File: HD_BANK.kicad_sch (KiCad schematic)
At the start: 1 part, among them J8 DF40HC(3.0)-120DS

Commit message: finishing schematic
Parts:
- removed J8: DF40HC(3.0)-120DS, Connector_Hirose_DF40:Hirose_DF40C-120DS-0.4V_2x60_P0.4mm, symbol dfdtc_Connector:Conn_02x60_Odd_Even
- added J6: FX8-140P-SV1, Connector_Hirose_FX8:Hirose_FX8-140P-SV_2x70_P0.6mm, symbol dfdtc_Connector:Conn_02x70_Odd_Even
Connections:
- new net +5V: J6.105 (Pin_105), J6.106 (Pin_106), J6.107 (Pin_107), J6.108 (Pin_108), J6.109 (Pin_109), J6.110 (Pin_110), J6.111 (Pin_111), J6.112 (Pin_112), J6.113 (Pin_113), J6.114 (Pin_114), J6.115 (Pin_115), J6.116 (Pin_116), J6.117 (Pin_117), J6.118 (Pin_118), J6.119 (Pin_119), J6.120 (Pin_120), J6.121, J6.122, J6.123, J6.124, J6.125, J6.126, J6.127, J6.128, J6.129, J6.130, J6.131, J6.132, J6.133, J6.134, J6.135, J6.136, J6.137, J6.138, J6.139, J6.140
- new net FAN_PWM: J6.87 (Pin_87)
- new net FAN_TACH: J6.89 (Pin_89)
- new net GND: J6.1 (Pin_1), J6.100 (Pin_100), J6.101 (Pin_101), J6.102 (Pin_102), J6.103 (Pin_103), J6.104 (Pin_104), J6.11 (Pin_11), J6.12 (Pin_12), J6.2 (Pin_2), J6.21 (Pin_21), J6.22 (Pin_22), J6.31 (Pin_31), J6.32 (Pin_32), J6.41 (Pin_41), J6.42 (Pin_42), J6.51 (Pin_51), J6.52 (Pin_52), J6.61 (Pin_61), J6.62 (Pin_62), J6.71 (Pin_71), J6.72 (Pin_72), J6.77 (Pin_77), J6.78 (Pin_78), J6.81 (Pin_81), J6.82 (Pin_82), J6.91 (Pin_91), J6.92 (Pin_92), J6.97 (Pin_97), J6.98 (Pin_98), J6.99 (Pin_99)
- new net IO_L10N_AD10N_87_N: J6.65 (Pin_65)
- new net IO_L10N_AD2N_84_N: J6.49 (Pin_49)
- new net IO_L10N_AD2N_86_N: J6.50 (Pin_50)
- new net IO_L10P_AD10P_87_P: J6.63 (Pin_63)
- new net IO_L10P_AD2P_84_P: J6.47 (Pin_47)
- new net IO_L10P_AD2P_86_P: J6.48 (Pin_48)
- new net IO_L11N_AD1N_84_N: J6.55 (Pin_55)
- new net IO_L11N_AD1N_86_N: J6.56 (Pin_56)
- new net IO_L11N_AD9N_87_N: J6.69 (Pin_69)
- new net IO_L11P_AD1P_84_P: J6.53 (Pin_53)
- new net IO_L11P_AD1P_86_P: J6.54 (Pin_54)
- new net IO_L11P_AD9P_87_P: J6.67 (Pin_67)
- new net IO_L12N_AD0N_84_N: J6.59 (Pin_59)
- new net IO_L12N_AD0N_86_N: J6.60 (Pin_60)
- new net IO_L12N_AD8N_87_N: J6.75 (Pin_75)
- new net IO_L12P_AD0P_84_P: J6.57 (Pin_57)
- new net IO_L12P_AD0P_86_P: J6.58 (Pin_58)
- new net IO_L12P_AD8P_87_P: J6.73 (Pin_73)
- new net IO_L1N_AD11N_84_N: J6.5 (Pin_5)
- new net IO_L1N_AD11N_86_N: J6.6 (Pin_6)
- new net IO_L1P_AD11P_84_P: J6.3 (Pin_3)
- new net IO_L1P_AD11P_86_P: J6.4 (Pin_4)
- new net IO_L2N_AD10N_84_N: J6.9 (Pin_9)
- new net IO_L2N_AD10N_86_N: J6.10 (Pin_10)
- new net IO_L2P_AD10P_84_P: J6.7 (Pin_7)
- new net IO_L2P_AD10P_86_P: J6.8 (Pin_8)
- new net IO_L3N_AD9N_84_N: J6.15 (Pin_15)
- new net IO_L3N_AD9N_86_N: J6.16 (Pin_16)
- new net IO_L3P_AD9P_84_P: J6.13 (Pin_13)
- new net IO_L3P_AD9P_86_P: J6.14 (Pin_14)
- new net IO_L4N_AD8N_84_N: J6.19 (Pin_19)
- new net IO_L4N_AD8N_86_N: J6.20 (Pin_20)
- new net IO_L4P_AD8P_84_P: J6.17 (Pin_17)
- new net IO_L4P_AD8P_86_P: J6.18 (Pin_18)
- new net IO_L5N_HDGC_AD7N_84_N: J6.25 (Pin_25)
- new net IO_L5N_HDGC_AD7N_86_N: J6.26 (Pin_26)
- new net IO_L5P_HDGC_AD7P_84_P: J6.23 (Pin_23)
- new net IO_L5P_HDGC_AD7P_86_P: J6.24 (Pin_24)
- new net IO_L6N_HDGC_87_N: J6.86 (Pin_86)
- new net IO_L6N_HDGC_AD6N_84_N: J6.29 (Pin_29)
- new net IO_L6N_HDGC_AD6N_86_N: J6.30 (Pin_30)
- new net IO_L6P_HDGC_AD6P_84_P: J6.27 (Pin_27)
- new net IO_L6P_HDGC_AD6P_86_P: J6.28 (Pin_28)
- new net IO_L7N_HDGC_87_N: J6.66 (Pin_66)
- new net IO_L7N_HDGC_AD5N_84_N: J6.35 (Pin_35)
- new net IO_L7N_HDGC_AD5N_86_N: J6.36 (Pin_36)
- new net IO_L7P_HDGC_87_P: J6.64 (Pin_64)
- new net IO_L7P_HDGC_AD5P_84_P: J6.33 (Pin_33)
- new net IO_L7P_HDGC_AD5P_86_P: J6.34 (Pin_34)
- new net IO_L8N_HDGC_87_N: J6.70 (Pin_70)
- new net IO_L8N_HDGC_AD4N_84_N: J6.39 (Pin_39)
- new net IO_L8N_HDGC_AD4N_86_N: J6.40 (Pin_40)
- new net IO_L8P_HDGC_87_P: J6.68 (Pin_68)
- new net IO_L8P_HDGC_AD4P_84_P: J6.37 (Pin_37)
- new net IO_L8P_HDGC_AD4P_86_P: J6.38 (Pin_38)
- new net IO_L9N_AD11N_87_N: J6.76 (Pin_76)
- new net IO_L9N_AD3N_84_N: J6.45 (Pin_45)
- new net IO_L9N_AD3N_86_N: J6.46 (Pin_46)
- new net IO_L9P_AD11P_87_P: J6.74 (Pin_74)
- new net IO_L9P_AD3P_84_P: J6.43 (Pin_43)
- new net IO_L9P_AD3P_86_P: J6.44 (Pin_44)
- new net P1_GPIO: J6.85 (Pin_85)
- new net P1_INT: J6.83 (Pin_83)
- new net PMIC_32KOUT: J6.84 (Pin_84)
- new net PMIC_PWRKY: J6.94 (Pin_94)
- new net Power_SCL: J6.90 (Pin_90)
- new net Power_SDA: J6.88 (Pin_88)
- new net VBAT: J6.96 (Pin_96)
- new net VCCO_HD: J6.79 (Pin_79), J6.80 (Pin_80)

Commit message: sync works
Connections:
- net GND: now also J6.105 (Pin_105), J6.106 (Pin_106), J6.107 (Pin_107), J6.108 (Pin_108), J6.109 (Pin_109), J6.110 (Pin_110), J6.111 (Pin_111), J6.112 (Pin_112), J6.113 (Pin_113), J6.114 (Pin_114), J6.115 (Pin_115), J6.116 (Pin_116), J6.117 (Pin_117), J6.118 (Pin_118), J6.119 (Pin_119), J6.120 (Pin_120), J6.121, J6.122
- net PROGRAM_B_0: now reaches J6.93 (Pin_93)
- net SYS_PG: now reaches J6.95 (Pin_95)
- net +5V renamed +12V
- net +12V: no longer J6.105 (Pin_105), J6.106 (Pin_106), J6.107 (Pin_107), J6.108 (Pin_108), J6.109 (Pin_109), J6.110 (Pin_110), J6.111 (Pin_111), J6.112 (Pin_112), J6.113 (Pin_113), J6.114 (Pin_114), J6.115 (Pin_115), J6.116 (Pin_116), J6.117 (Pin_117), J6.118 (Pin_118), J6.119 (Pin_119), J6.120 (Pin_120), J6.121, J6.122

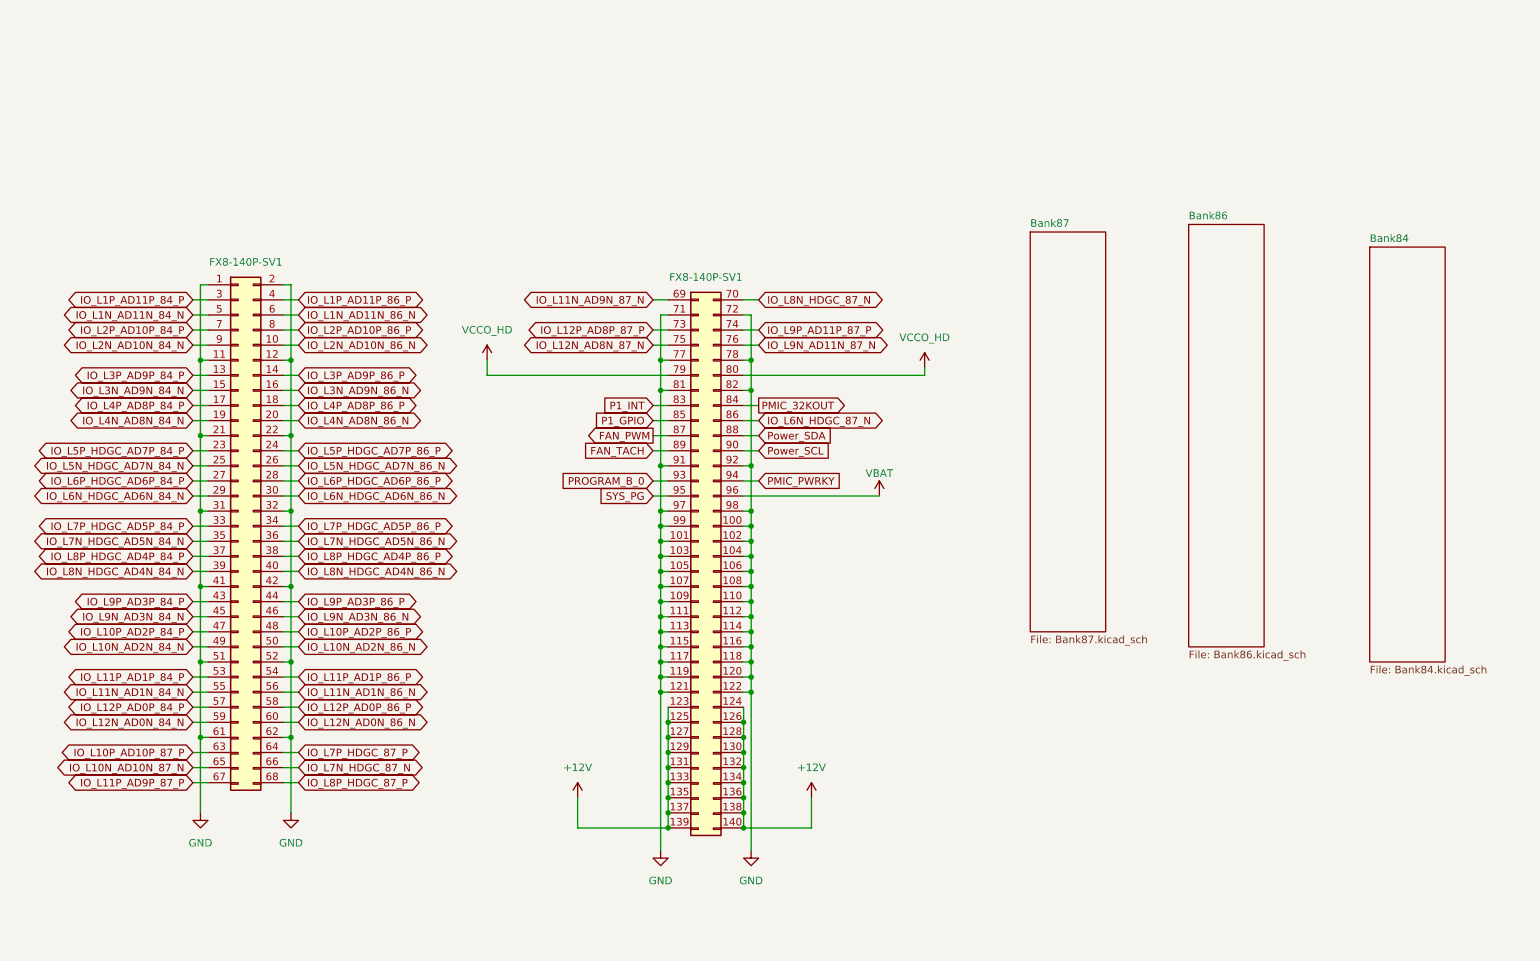
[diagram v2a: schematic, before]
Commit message: change net name to of IO diff pairs, add a scripts for name modification
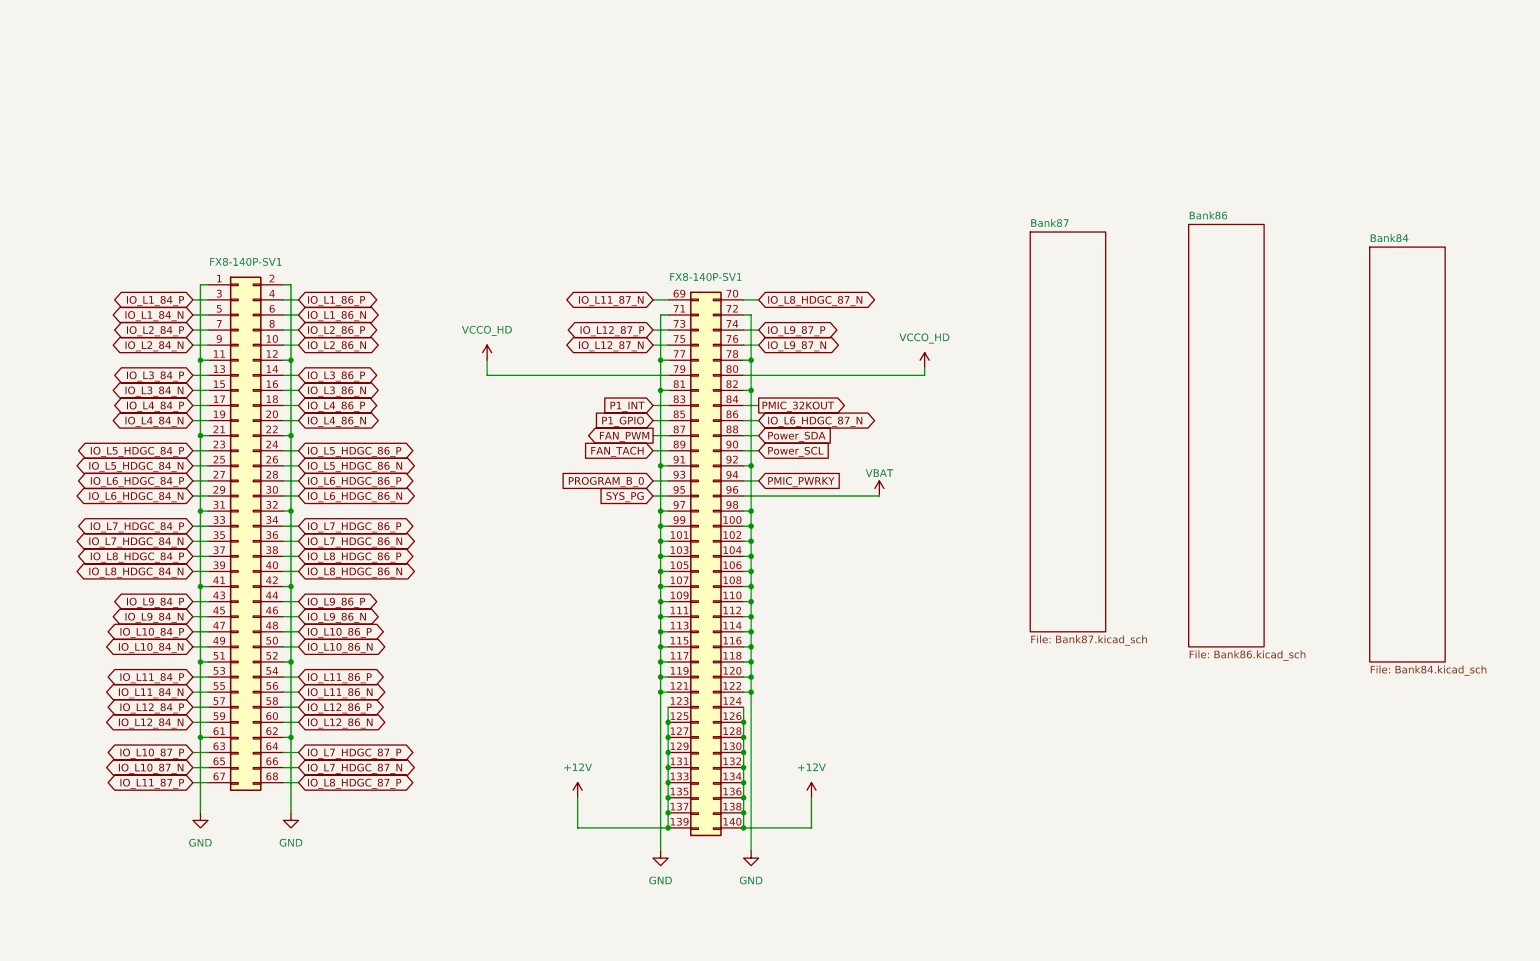
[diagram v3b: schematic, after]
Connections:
- net IO_L10N_AD10N_87_N renamed IO_L10_87_N
- net IO_L10N_AD2N_84_N renamed IO_L10_84_N
- net IO_L10N_AD2N_86_N renamed IO_L10_86_N
- net IO_L10P_AD10P_87_P renamed IO_L10_87_P
- net IO_L10P_AD2P_84_P renamed IO_L10_84_P
- net IO_L10P_AD2P_86_P renamed IO_L10_86_P
- net IO_L11N_AD1N_84_N renamed IO_L11_84_N
- net IO_L11N_AD1N_86_N renamed IO_L11_86_N
- net IO_L11N_AD9N_87_N renamed IO_L11_87_N
- net IO_L11P_AD1P_84_P renamed IO_L11_84_P
- net IO_L11P_AD1P_86_P renamed IO_L11_86_P
- net IO_L11P_AD9P_87_P renamed IO_L11_87_P
- net IO_L12N_AD0N_84_N renamed IO_L12_84_N
- net IO_L12N_AD0N_86_N renamed IO_L12_86_N
- net IO_L12N_AD8N_87_N renamed IO_L12_87_N
- net IO_L12P_AD0P_84_P renamed IO_L12_84_P
- net IO_L12P_AD0P_86_P renamed IO_L12_86_P
- net IO_L12P_AD8P_87_P renamed IO_L12_87_P
- net IO_L1N_AD11N_84_N renamed IO_L1_84_N
- net IO_L1N_AD11N_86_N renamed IO_L1_86_N
- net IO_L1P_AD11P_84_P renamed IO_L1_84_P
- net IO_L1P_AD11P_86_P renamed IO_L1_86_P
- net IO_L2N_AD10N_84_N renamed IO_L2_84_N
- net IO_L2N_AD10N_86_N renamed IO_L2_86_N
- net IO_L2P_AD10P_84_P renamed IO_L2_84_P
- net IO_L2P_AD10P_86_P renamed IO_L2_86_P
- net IO_L3N_AD9N_84_N renamed IO_L3_84_N
- net IO_L3N_AD9N_86_N renamed IO_L3_86_N
- net IO_L3P_AD9P_84_P renamed IO_L3_84_P
- net IO_L3P_AD9P_86_P renamed IO_L3_86_P
- net IO_L4N_AD8N_84_N renamed IO_L4_84_N
- net IO_L4N_AD8N_86_N renamed IO_L4_86_N
- net IO_L4P_AD8P_84_P renamed IO_L4_84_P
- net IO_L4P_AD8P_86_P renamed IO_L4_86_P
- net IO_L5N_HDGC_AD7N_84_N renamed IO_L5_HDGC_84_N
- net IO_L5N_HDGC_AD7N_86_N renamed IO_L5_HDGC_86_N
- net IO_L5P_HDGC_AD7P_84_P renamed IO_L5_HDGC_84_P
- net IO_L5P_HDGC_AD7P_86_P renamed IO_L5_HDGC_86_P
- net IO_L6N_HDGC_87_N renamed IO_L6_HDGC_87_N
- net IO_L6N_HDGC_AD6N_84_N renamed IO_L6_HDGC_84_N
- net IO_L6N_HDGC_AD6N_86_N renamed IO_L6_HDGC_86_N
- net IO_L6P_HDGC_AD6P_84_P renamed IO_L6_HDGC_84_P
- net IO_L6P_HDGC_AD6P_86_P renamed IO_L6_HDGC_86_P
- net IO_L7N_HDGC_87_N renamed IO_L7_HDGC_87_N
- net IO_L7N_HDGC_AD5N_84_N renamed IO_L7_HDGC_84_N
- net IO_L7N_HDGC_AD5N_86_N renamed IO_L7_HDGC_86_N
- net IO_L7P_HDGC_87_P renamed IO_L7_HDGC_87_P
- net IO_L7P_HDGC_AD5P_84_P renamed IO_L7_HDGC_84_P
- net IO_L7P_HDGC_AD5P_86_P renamed IO_L7_HDGC_86_P
- net IO_L8N_HDGC_87_N renamed IO_L8_HDGC_87_N
- net IO_L8N_HDGC_AD4N_84_N renamed IO_L8_HDGC_84_N
- net IO_L8N_HDGC_AD4N_86_N renamed IO_L8_HDGC_86_N
- net IO_L8P_HDGC_87_P renamed IO_L8_HDGC_87_P
- net IO_L8P_HDGC_AD4P_84_P renamed IO_L8_HDGC_84_P
- net IO_L8P_HDGC_AD4P_86_P renamed IO_L8_HDGC_86_P
- net IO_L9N_AD11N_87_N renamed IO_L9_87_N
- net IO_L9N_AD3N_84_N renamed IO_L9_84_N
- net IO_L9N_AD3N_86_N renamed IO_L9_86_N
- net IO_L9P_AD11P_87_P renamed IO_L9_87_P
- net IO_L9P_AD3P_84_P renamed IO_L9_84_P
- net IO_L9P_AD3P_86_P renamed IO_L9_86_P
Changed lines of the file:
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@@
 		)
 	)
-	(global_label "IO_L3P_AD9P_84_P"
+	(global_label "IO_L3_84_P"
 		(shape bidirectional)
 		(at 55.88 95.25 180)
@@
 		)
 	)
-	(global_label "IO_L4P_AD8P_84_P"
+	(global_label "IO_L4_84_P"
 		(shape bidirectional)
 		(at 55.88 100.33 180)
@@
 		)
 	)
-	(global_label "IO_L1N_AD11N_86_N"
+	(global_label "IO_L1_86_N"
 		(shape bidirectional)
 		(at 73.66 85.09 0)
@@
 		)
 	)
-	(global_label "IO_L7N_HDGC_87_N"
+	(global_label "IO_L7_HDGC_87_N"
 		(shape bidirectional)
 		(at 73.66 161.29 0)
@@
 		)
 	)
-	(global_label "IO_L9N_AD11N_87_N"
+	(global_label "IO_L9_87_N"
 		(shape bidirectional)
 		(at 151.13 90.17 0)
@@
 		)
 	)
-	(global_label "IO_L9P_AD11P_87_P"
+	(global_label "IO_L9_87_P"
 		(shape bidirectional)
 		(at 151.13 87.63 0)
@@
 		)
 	)
-	(global_label "IO_L5N_HDGC_AD7N_86_N"
+	(global_label "IO_L5_HDGC_86_N"
 		(shape bidirectional)
 		(at 73.66 110.49 0)
@@
 		)
 	)
-	(global_label "IO_L6P_HDGC_AD6P_86_P"
+	(global_label "IO_L6_HDGC_86_P"
 		(shape bidirectional)
 		(at 73.66 113.03 0)
@@
 		)
 	)
-	(global_label "IO_L6N_HDGC_87_N"
+	(global_label "IO_L6_HDGC_87_N"
 		(shape bidirectional)
 		(at 151.13 102.87 0)
@@
 		)
 	)
-	(global_label "IO_L12N_AD8N_87_N"
+	(global_label "IO_L12_87_N"
 		(shape bidirectional)
 		(at 133.35 90.17 180)
@@
 		)
 	)
-	(global_label "IO_L11P_AD1P_84_P"
+	(global_label "IO_L11_84_P"
 		(shape bidirectional)
 		(at 55.88 146.05 180)
@@
 		)
 	)
-	(global_label "IO_L8P_HDGC_AD4P_86_P"
+	(global_label "IO_L8_HDGC_86_P"
 		(shape bidirectional)
 		(at 73.66 125.73 0)
@@
 		)
 	)
-	(global_label "IO_L4N_AD8N_86_N"
+	(global_label "IO_L4_86_N"
 		(shape bidirectional)
 		(at 73.66 102.87 0)
@@
 		)
 	)
-	(global_label "IO_L9P_AD3P_86_P"
+	(global_label "IO_L9_86_P"
 		(shape bidirectional)
 		(at 73.66 133.35 0)
@@
 		)
 	)
-	(global_label "IO_L7P_HDGC_AD5P_86_P"
+	(global_label "IO_L7_HDGC_86_P"
 		(shape bidirectional)
 		(at 73.66 120.65 0)
@@
 		)
 	)
-	(global_label "IO_L2P_AD10P_84_P"
+	(global_label "IO_L2_84_P"
 		(shape bidirectional)
 		(at 55.88 87.63 180)
@@
 		)
 	)
-	(global_label "IO_L8N_HDGC_AD4N_84_N"
+	(global_label "IO_L8_HDGC_84_N"
 		(shape bidirectional)
 		(at 55.88 128.27 180)
@@
 		)
 	)
-	(global_label "IO_L10N_AD2N_86_N"
+	(global_label "IO_L10_86_N"
 		(shape bidirectional)
 		(at 73.66 140.97 0)
@@
 		)
 	)
-	(global_label "IO_L12N_AD0N_84_N"
+	(global_label "IO_L12_84_N"
 		(shape bidirectional)
 		(at 55.88 153.67 180)
@@
 		)
 	)
-	(global_label "IO_L11N_AD1N_84_N"
+	(global_label "IO_L11_84_N"
 		(shape bidirectional)
 		(at 55.88 148.59 180)
@@
 		)
 	)
-	(global_label "IO_L7N_HDGC_AD5N_86_N"
+	(global_label "IO_L7_HDGC_86_N"
 		(shape bidirectional)
 		(at 73.66 123.19 0)
@@
 		)
 	)
-	(global_label "IO_L7N_HDGC_AD5N_84_N"
+	(global_label "IO_L7_HDGC_84_N"
 		(shape bidirectional)
 		(at 55.88 123.19 180)
@@
 		)
 	)
-	(global_label "IO_L12P_AD0P_84_P"
+	(global_label "IO_L12_84_P"
 		(shape bidirectional)
 		(at 55.88 151.13 180)
@@
 		)
 	)
-	(global_label "IO_L11P_AD1P_86_P"
+	(global_label "IO_L11_86_P"
 		(shape bidirectional)
 		(at 73.66 146.05 0)
@@
 		)
 	)
-	(global_label "IO_L10P_AD10P_87_P"
+	(global_label "IO_L10_87_P"
 		(shape bidirectional)
 		(at 55.88 158.75 180)
@@
 		)
 	)
-	(global_label "IO_L11N_AD9N_87_N"
+	(global_label "IO_L11_87_N"
 		(shape bidirectional)
 		(at 133.35 82.55 180)
@@
 		)
 	)
-	(global_label "IO_L1P_AD11P_84_P"
+	(global_label "IO_L1_84_P"
 		(shape bidirectional)
 		(at 55.88 82.55 180)
@@
 		)
 	)
-	(global_label "IO_L4N_AD8N_84_N"
+	(global_label "IO_L4_84_N"
 		(shape bidirectional)
 		(at 55.88 102.87 180)
@@
 		)
 	)
-	(global_label "IO_L4P_AD8P_86_P"
+	(global_label "IO_L4_86_P"
 		(shape bidirectional)
 		(at 73.66 100.33 0)
@@
 		)
 	)
-	(global_label "IO_L3P_AD9P_86_P"
+	(global_label "IO_L3_86_P"
 		(shape bidirectional)
 		(at 73.66 95.25 0)
@@
 		)
 	)
-	(global_label "IO_L10N_AD10N_87_N"
+	(global_label "IO_L10_87_N"
 		(shape bidirectional)
 		(at 55.88 161.29 180)
@@
 		)
 	)
-	(global_label "IO_L11P_AD9P_87_P"
+	(global_label "IO_L11_87_P"
 		(shape bidirectional)
 		(at 55.88 163.83 180)
@@
 		)
 	)
-	(global_label "IO_L2N_AD10N_86_N"
+	(global_label "IO_L2_86_N"
 		(shape bidirectional)
 		(at 73.66 90.17 0)
@@
 		)
 	)
-	(global_label "IO_L2P_AD10P_86_P"
+	(global_label "IO_L2_86_P"
 		(shape bidirectional)
 		(at 73.66 87.63 0)
@@
 		)
 	)
-	(global_label "IO_L3N_AD9N_86_N"
+	(global_label "IO_L3_86_N"
 		(shape bidirectional)
 		(at 73.66 97.79 0)
@@
 		)
 	)
-	(global_label "IO_L12N_AD0N_86_N"
+	(global_label "IO_L12_86_N"
 		(shape bidirectional)
 		(at 73.66 153.67 0)
@@
 		)
 	)
-	(global_label "IO_L8P_HDGC_AD4P_84_P"
+	(global_label "IO_L8_HDGC_84_P"
 		(shape bidirectional)
 		(at 55.88 125.73 180)
@@
 		)
 	)
-	(global_label "IO_L9P_AD3P_84_P"
+	(global_label "IO_L9_84_P"
 		(shape bidirectional)
 		(at 55.88 133.35 180)
@@
 		)
 	)
-	(global_label "IO_L7P_HDGC_87_P"
+	(global_label "IO_L7_HDGC_87_P"
 		(shape bidirectional)
 		(at 73.66 158.75 0)
@@
 		)
 	)
-	(global_label "IO_L5P_HDGC_AD7P_84_P"
+	(global_label "IO_L5_HDGC_84_P"
 		(shape bidirectional)
 		(at 55.88 107.95 180)
@@
 		)
 	)
-	(global_label "IO_L8N_HDGC_87_N"
+	(global_label "IO_L8_HDGC_87_N"
 		(shape bidirectional)
 		(at 151.13 82.55 0)
@@
 		)
 	)
-	(global_label "IO_L3N_AD9N_84_N"
+	(global_label "IO_L3_84_N"
 		(shape bidirectional)
 		(at 55.88 97.79 180)
@@
 		)
 	)
-	(global_label "IO_L9N_AD3N_86_N"
+	(global_label "IO_L9_86_N"
 		(shape bidirectional)
 		(at 73.66 135.89 0)
@@
 		)
 	)
-	(global_label "IO_L11N_AD1N_86_N"
+	(global_label "IO_L11_86_N"
 		(shape bidirectional)
 		(at 73.66 148.59 0)
@@
 		)
 	)
-	(global_label "IO_L7P_HDGC_AD5P_84_P"
+	(global_label "IO_L7_HDGC_84_P"
 		(shape bidirectional)
 		(at 55.88 120.65 180)
@@
 		)
 	)
-	(global_label "IO_L12P_AD8P_87_P"
+	(global_label "IO_L12_87_P"
 		(shape bidirectional)
 		(at 133.35 87.63 180)
@@
 		)
 	)
-	(global_label "IO_L6P_HDGC_AD6P_84_P"
+	(global_label "IO_L6_HDGC_84_P"
 		(shape bidirectional)
 		(at 55.88 113.03 180)
@@
 		)
 	)
-	(global_label "IO_L10P_AD2P_86_P"
+	(global_label "IO_L10_86_P"
 		(shape bidirectional)
 		(at 73.66 138.43 0)
@@
 		)
 	)
-	(global_label "IO_L9N_AD3N_84_N"
+	(global_label "IO_L9_84_N"
 		(shape bidirectional)
 		(at 55.88 135.89 180)
@@
 		)
 	)
-	(global_label "IO_L1P_AD11P_86_P"
+	(global_label "IO_L1_86_P"
 		(shape bidirectional)
 		(at 73.66 82.55 0)
@@
 		)
 	)
-	(global_label "IO_L5N_HDGC_AD7N_84_N"
+	(global_label "IO_L5_HDGC_84_N"
 		(shape bidirectional)
 		(at 55.88 110.49 180)
@@
 		)
 	)
-	(global_label "IO_L5P_HDGC_AD7P_86_P"
+	(global_label "IO_L5_HDGC_86_P"
 		(shape bidirectional)
 		(at 73.66 107.95 0)
@@
 		)
 	)
-	(global_label "IO_L10P_AD2P_84_P"
+	(global_label "IO_L10_84_P"
 		(shape bidirectional)
 		(at 55.88 138.43 180)
@@
 		)
 	)
-	(global_label "IO_L6N_HDGC_AD6N_84_N"
+	(global_label "IO_L6_HDGC_84_N"
 		(shape bidirectional)
 		(at 55.88 115.57 180)
@@
 		)
 	)
-	(global_label "IO_L8P_HDGC_87_P"
+	(global_label "IO_L8_HDGC_87_P"
 		(shape bidirectional)
 		(at 73.66 163.83 0)
@@
 		)
 	)
-	(global_label "IO_L6N_HDGC_AD6N_86_N"
+	(global_label "IO_L6_HDGC_86_N"
 		(shape bidirectional)
 		(at 73.66 115.57 0)
@@
 		)
 	)
-	(global_label "IO_L10N_AD2N_84_N"
+	(global_label "IO_L10_84_N"
 		(shape bidirectional)
 		(at 55.88 140.97 180)
@@
 		)
 	)
-	(global_label "IO_L2N_AD10N_84_N"
+	(global_label "IO_L2_84_N"
 		(shape bidirectional)
 		(at 55.88 90.17 180)
@@
 		)
 	)
-	(global_label "IO_L1N_AD11N_84_N"
+	(global_label "IO_L1_84_N"
 		(shape bidirectional)
 		(at 55.88 85.09 180)
@@
 		)
 	)
-	(global_label "IO_L8N_HDGC_AD4N_86_N"
+	(global_label "IO_L8_HDGC_86_N"
 		(shape bidirectional)
 		(at 73.66 128.27 0)
@@
 		)
 	)
-	(global_label "IO_L12P_AD0P_86_P"
+	(global_label "IO_L12_86_P"
 		(shape bidirectional)
 		(at 73.66 151.13 0)
